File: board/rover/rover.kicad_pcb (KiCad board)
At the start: 2 copper layers, 107 x 60 mm, 46 parts, among them U1 MCP6022, U2 LM393, U3 MCP6022, U4 TLE2072CP

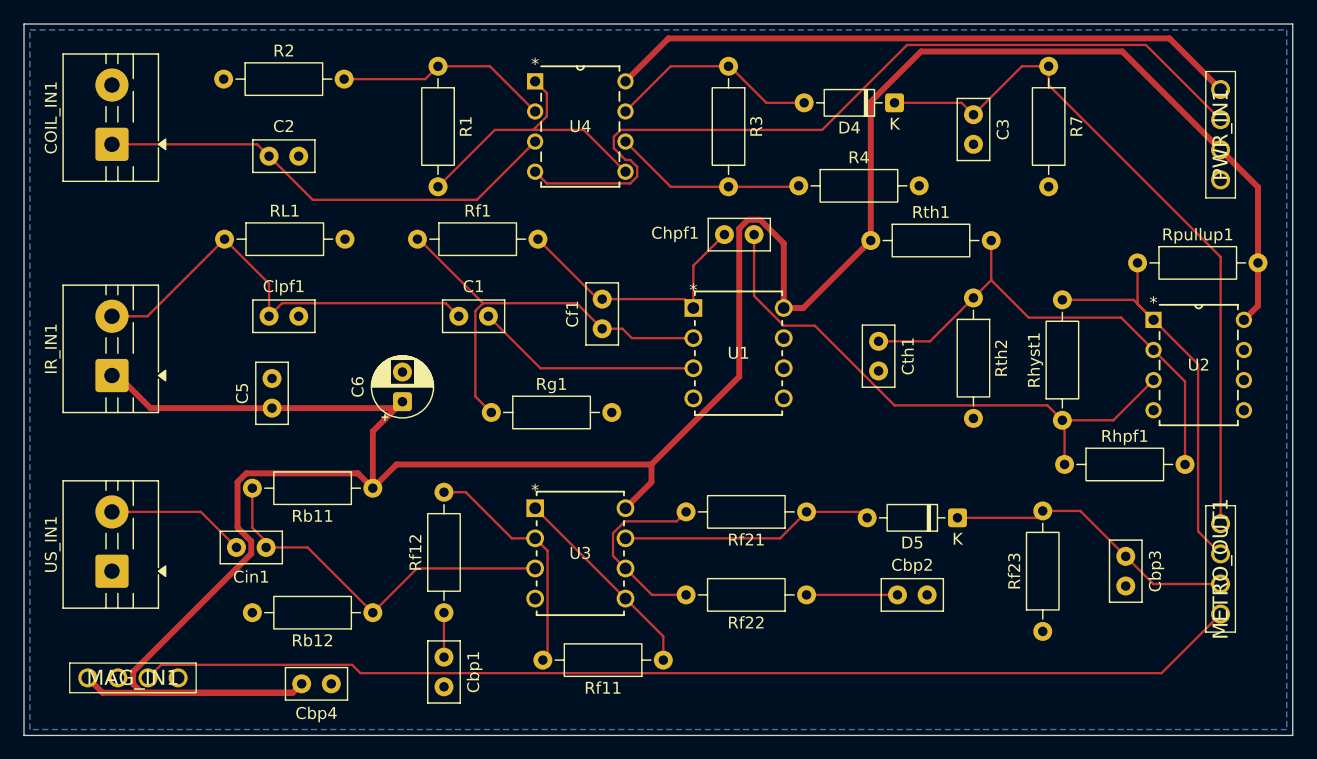
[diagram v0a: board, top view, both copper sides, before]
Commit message: Added -5V generation to PCB
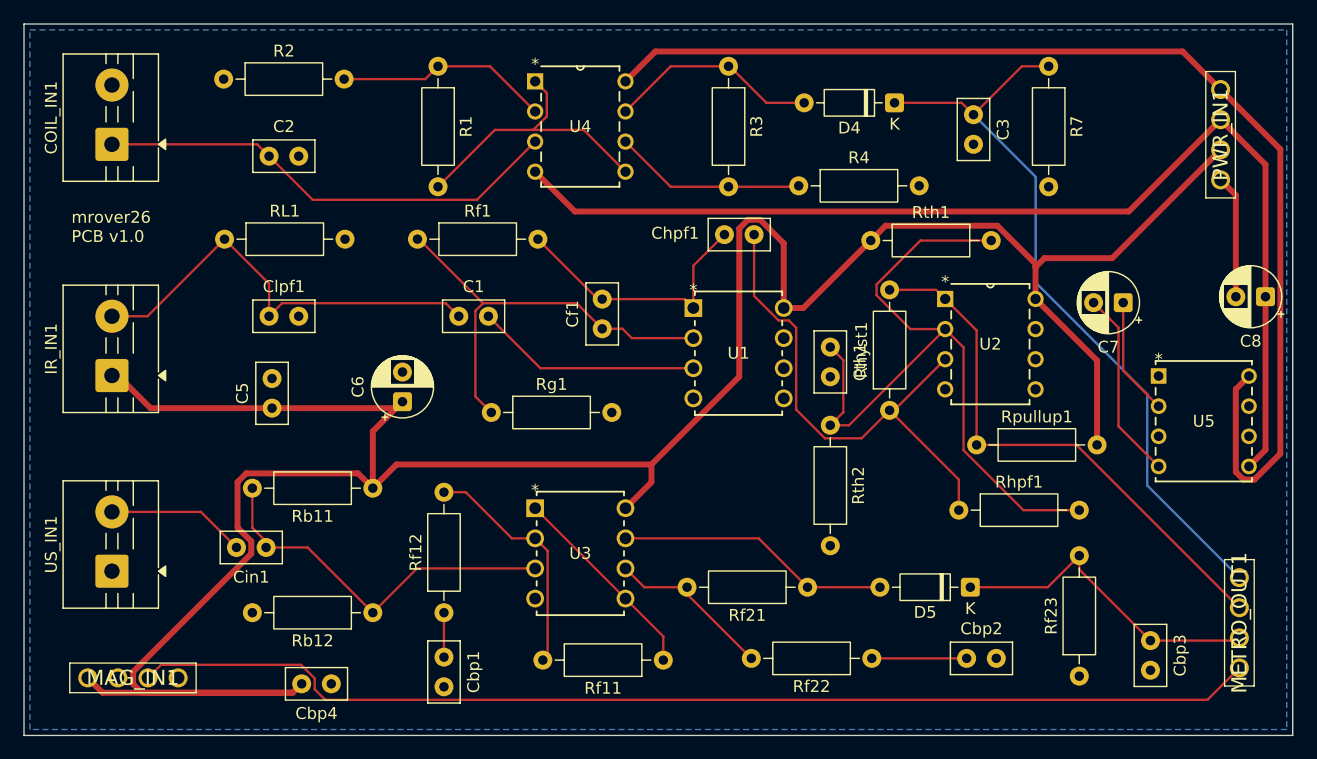
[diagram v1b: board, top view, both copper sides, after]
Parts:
- added C7: 10u, Capacitor_THT:CP_Radial_D5.0mm_P2.50mm, F.Cu at (185.7, 78.5)
- added C8: 10u, Capacitor_THT:CP_Radial_D5.0mm_P2.50mm, F.Cu at (197.7, 78.0)
- added U5: icl7660cpa, ICL7660CPA:21-0043D_8_MXM, F.Cu at (188.7, 84.7)
- moved Rpullup1 20.5 mm to (173.3, 90.5)
- moved U2 17.7 mm to (178.3, 85.8)
- moved Rth2 16.2 mm to (161.0, 88.8)
- moved Rhyst1 14.6 mm to (166.0, 87.6)
- moved Rhpf1 9.71 mm to (171.8, 96.0)
- moved Cbp2 7.92 mm to (172.5, 108.5)
- moved Rf22 7.68 mm to (164.5, 108.5)
- moved Cbp3 7.40 mm to (188.0, 107.0)
- moved Rf21 6.35 mm to (159.1, 102.5)
- moved D5 5.95 mm to (172.8, 102.5)
- moved Rf23 4.87 mm to (182.0, 110.0)
- moved METRO_OUT1 4.81 mm to (195.5, 101.7)
- moved Cth1 4.10 mm to (161.0, 82.2)
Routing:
- net +5V: track 53.5 -> 98.8 mm
- net -5V: track 70.6 -> 93.8 mm
- net Net-(U2A--): track 41.9 -> 62.4 mm
- net Net-(U5-CAP-): track 0.00 -> 16.1 mm
- net /IR_OUT: track 35.8 -> 46.3 mm
- net GND: track 0.00 -> 10.4 mm
- net Net-(U5-CAP+): track 0.00 -> 9.97 mm
- net +3.3V: track 235.2 -> 225.5 mm
- net Net-(U2A-+): track 48.4 -> 43.9 mm
- net /AGE_OUT: track 59.7 -> 63.4 mm
- net /US_OUT: track 25.0 -> 27.5 mm
- net Net-(U3B--): track 16.3 -> 14.1 mm
- net /MAG_OUT: track 93.3 -> 95.4 mm
- net Net-(D5-A): track 21.5 -> 23.2 mm
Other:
- board text added: "mrover26 PCB v1.0"
